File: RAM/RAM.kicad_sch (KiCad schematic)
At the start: 0 parts

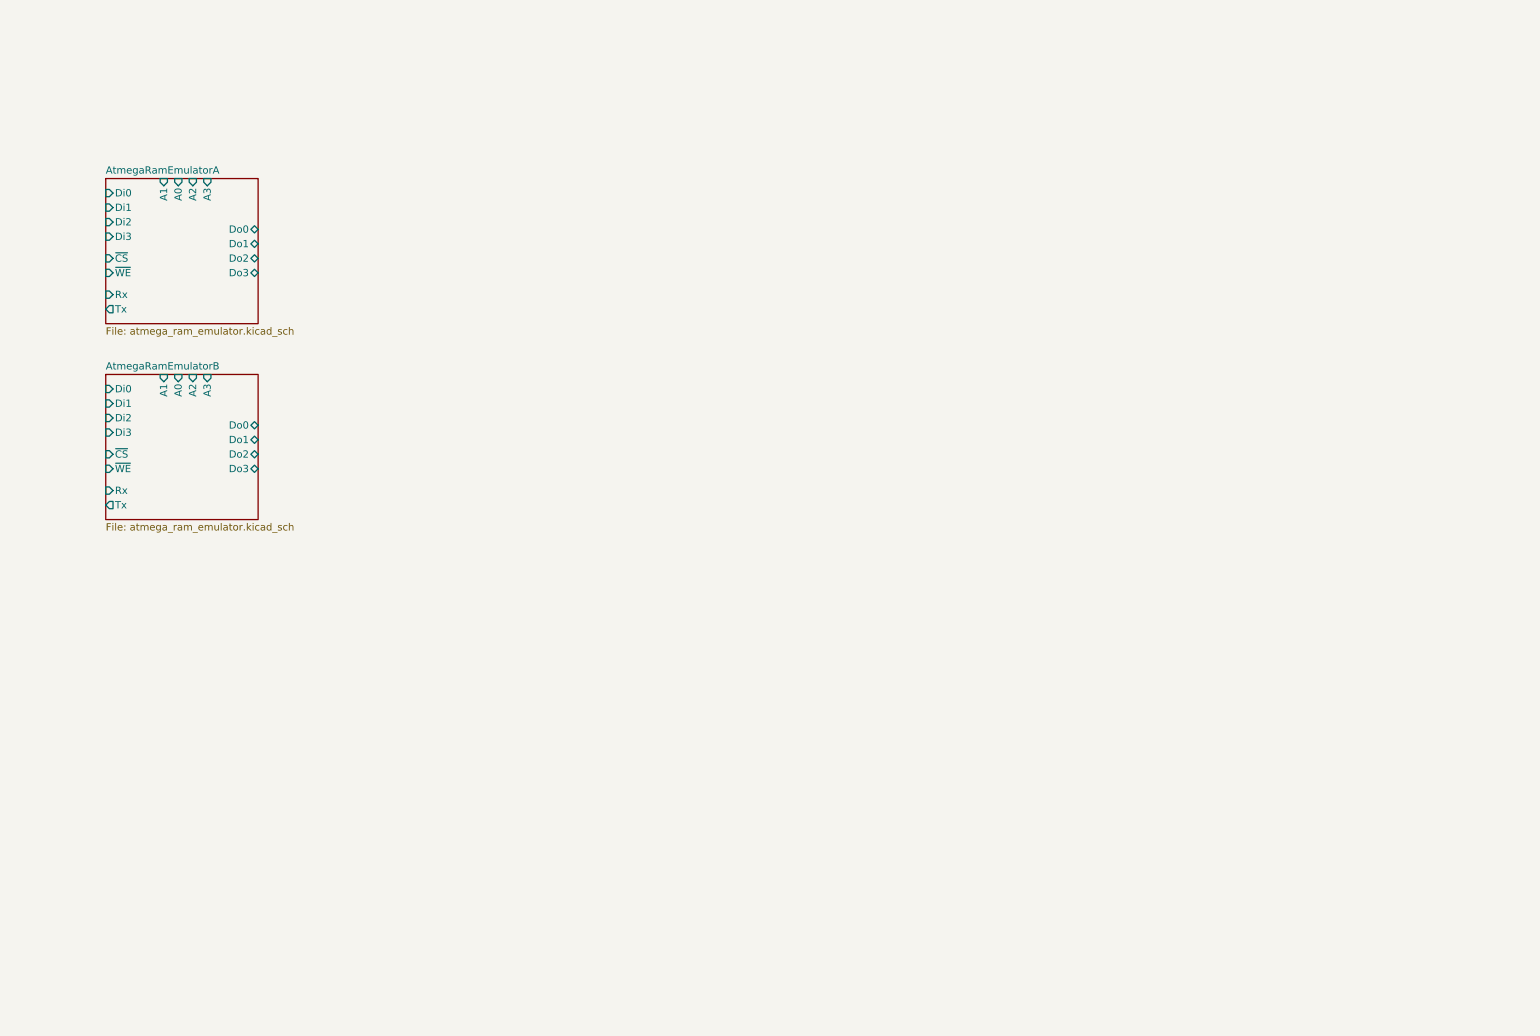
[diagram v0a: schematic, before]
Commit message: RAM input selection schematic complete
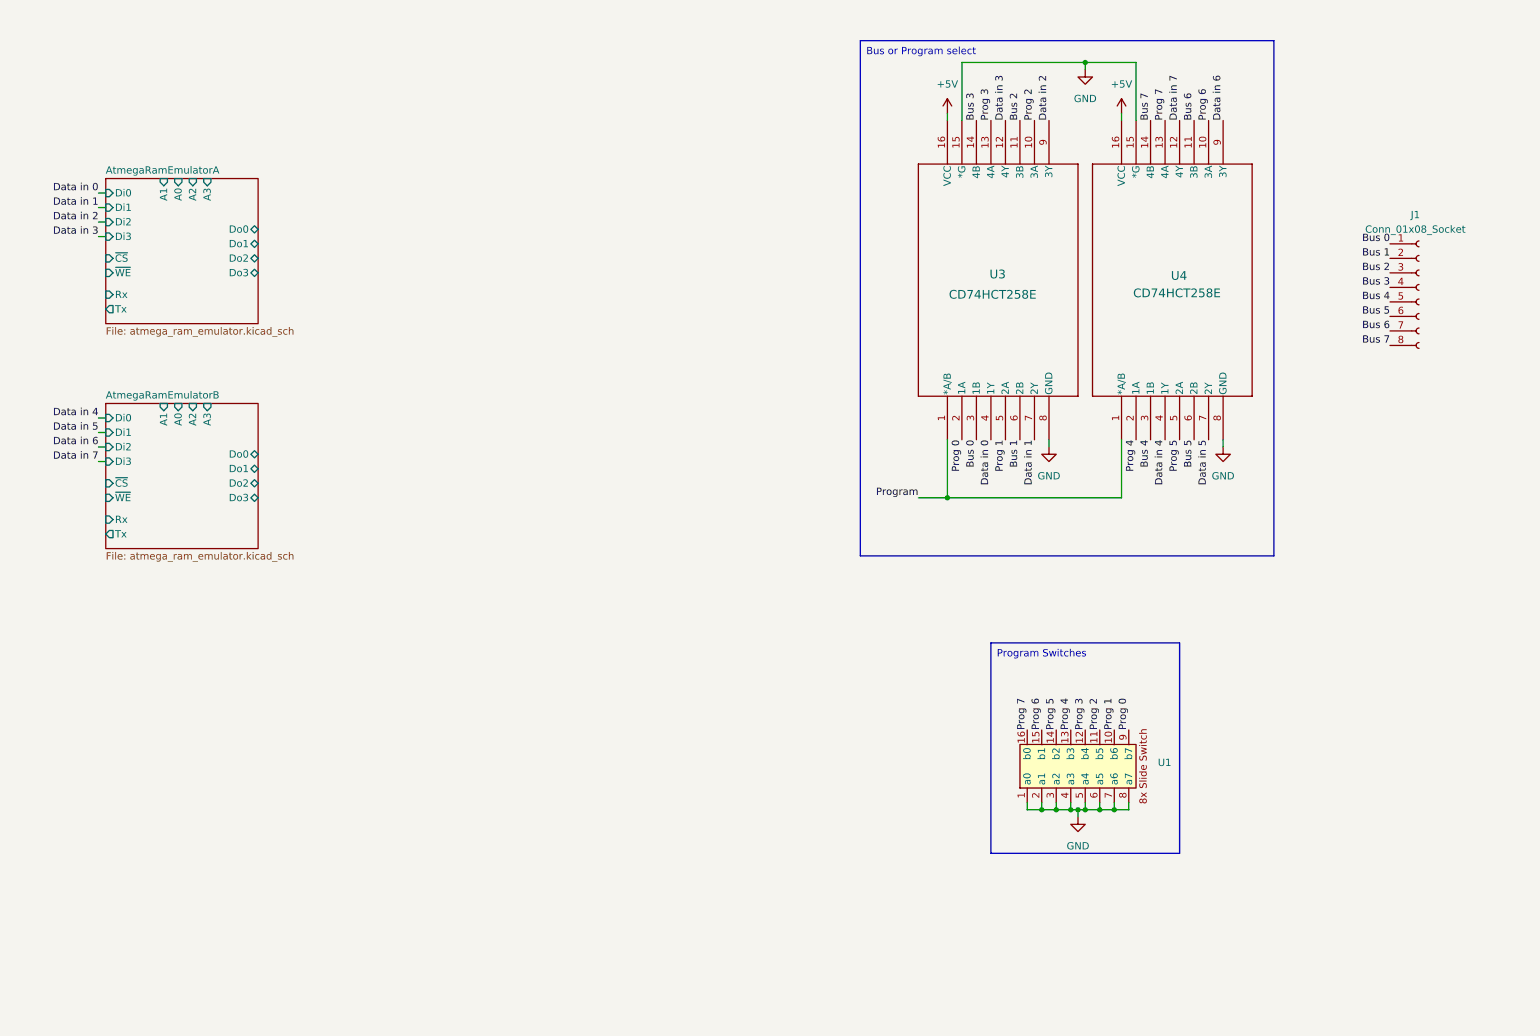
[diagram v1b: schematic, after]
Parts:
- added J1: Conn_01x08_Socket, Connector_PinHeader_1.00mm:PinHeader_1x08_P1.00mm_Horizontal, symbol Connector:Conn_01x08_Socket
- added U1: ~, symbol 8BitCPU:8x_slide_switch
- added U3, U4: CD74HCT258E, N16, symbol 2_to_1_selector:CD74HCT258E
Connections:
- new net +5V: U3.16 (VCC), U4.16 (VCC)
- new net Bus 0: J1.1 (Pin_1), U3.3 (1B)
- new net Bus 1: J1.2 (Pin_2), U3.6 (2B)
- new net Bus 2: J1.3 (Pin_3), U3.11 (3B)
- new net Bus 3: J1.4 (Pin_4), U3.14 (4B)
- new net Bus 4: J1.5 (Pin_5), U4.3 (1B)
- new net Bus 5: J1.6 (Pin_6), U4.6 (2B)
- new net Bus 6: J1.7 (Pin_7), U4.11 (3B)
- new net Bus 7: J1.8 (Pin_8), U4.14 (4B)
- new net Data in 0: U3.4 (1Y)
- new net Data in 1: U3.7 (2Y)
- new net Data in 2: U3.9 (3Y)
- new net Data in 3: U3.12 (4Y)
- new net Data in 4: U4.4 (1Y)
- new net Data in 5: U4.7 (2Y)
- new net Data in 6: U4.9 (3Y)
- new net Data in 7: U4.12 (4Y)
- new net GND: U1.1 (a0), U1.2 (a1), U1.3 (a2), U1.4 (a3), U1.5 (a4), U1.6 (a5), U1.7 (a6), U1.8 (a7), U3.15 (*G), U3.8 (GND), U4.15 (*G), U4.8 (GND)
- new net Prog 0: U1.9 (b7), U3.2 (1A)
- new net Prog 1: U1.10 (b6), U3.5 (2A)
- new net Prog 2: U1.11 (b5), U3.10 (3A)
- new net Prog 3: U1.12 (b4), U3.13 (4A)
- new net Prog 4: U1.13 (b3), U4.2 (1A)
- new net Prog 5: U1.14 (b2), U4.5 (2A)
- new net Prog 6: U1.15 (b1), U4.10 (3A)
- new net Prog 7: U1.16 (b0), U4.13 (4A)
- new net Program: U3.1 (*A/B), U4.1 (*A/B)

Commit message: RAM output connected to bus
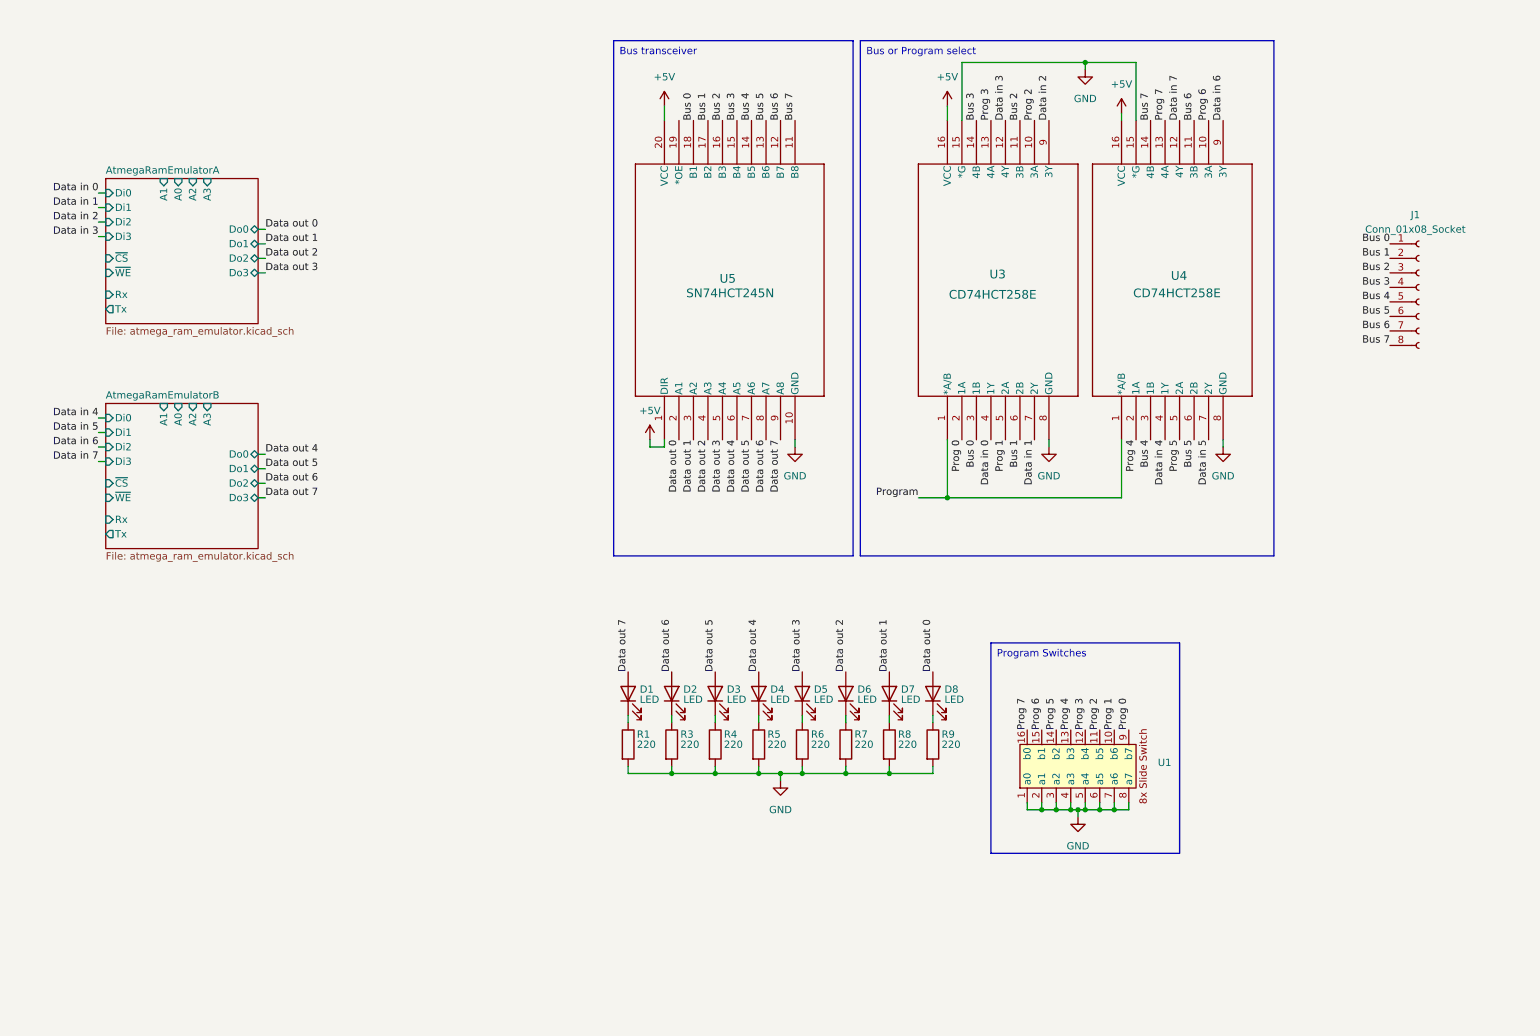
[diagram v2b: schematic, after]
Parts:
- added D1, D2, D3, D4, D5, D6, D7, D8: LED, LED_THT:LED_D2.0mm_W4.8mm_H2.5mm_FlatTop, symbol Device:LED
- added R1, R3, R4, R5, R6, R7, R8, R9: 220, _DownloadFootprints:CF_series_Resistors_THT, symbol Device:R
- added U5: SN74HCT245N, _DownloadFootprints:8x_tristate_transceiver, symbol 8x_tristate_transceiver:SN74HCT245N
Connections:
- net +5V: now also U5.1 (DIR), U5.20 (VCC)
- net Bus 0: now also U5.18 (B1)
- net Bus 1: now also U5.17 (B2)
- net Bus 2: now also U5.16 (B3)
- net Bus 3: now also U5.15 (B4)
- net Bus 4: now also U5.14 (B5)
- net Bus 5: now also U5.13 (B6)
- net Bus 6: now also U5.12 (B7)
- net Bus 7: now also U5.11 (B8)
- net GND: now also R1.2, R3.2, R4.2, R5.2, R6.2, R7.2, R8.2, R9.2, U5.10 (GND)
- new net: D7.1 (K), R8.1
- new net: D8.1 (K), R9.1
- new net: D4.1 (K), R5.1
- new net: D1.1 (K), R1.1
- new net: D6.1 (K), R7.1
- new net: D2.1 (K), R3.1
- new net: D3.1 (K), R4.1
- new net: D5.1 (K), R6.1
- new net Data out 0: D8.2 (A), U5.2 (A1)
- new net Data out 1: D7.2 (A), U5.3 (A2)
- new net Data out 2: D6.2 (A), U5.4 (A3)
- new net Data out 3: D5.2 (A), U5.5 (A4)
- new net Data out 4: D4.2 (A), U5.6 (A5)
- new net Data out 5: D3.2 (A), U5.7 (A6)
- new net Data out 6: D2.2 (A), U5.8 (A7)
- new net Data out 7: D1.2 (A), U5.9 (A8)

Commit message: Added logic to select between program or run mode signals
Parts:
- added C1: C, symbol Device:C
- added J2, J3: Conn_01x02_Pin, symbol Connector:Conn_01x02_Pin
- added J4: Conn_01x04_Pin, symbol Connector:Conn_01x04_Pin
- added R10: R, symbol Device:R
- added S1: B3U-1000P, _DownloadFootprints:tactile_switch, symbol dk_Tactile-Switches:B3U-1000P
- added U6: CD74HCT258E, N16, symbol 2_to_1_selector:CD74HCT258E
- added U7: ~, symbol 8BitCPU:4x_and
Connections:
- net +5V: now also U6.16 (VCC), U7.14 (VCC)
- net AtmegaRamEmulatorA/Rx: now also J3.1 (Pin_1)
- net AtmegaRamEmulatorA/Tx: now also J3.2 (Pin_2)
- net AtmegaRamEmulatorA/~{WE}: now also U6.12 (4Y)
- net AtmegaRamEmulatorB/Rx: now also J2.1 (Pin_1)
- net AtmegaRamEmulatorB/Tx: now also J2.2 (Pin_2)
- net GND: now also R10.2, S1.2, U6.15 (*G), U6.8 (GND), U7.7 (GND)
- net Program: now also J4.1 (Pin_1), U6.1 (*A/B)
- new net: C1.2, R10.1, U7.1 (1A)
- new net: S1.1, U6.13 (4A)
- new net: U6.14 (4B), U7.3 (1Y)
- new net CLK: C1.1, J4.2 (Pin_2)
- new net Read in: J4.4 (Pin_4), U7.2 (1B)
- new net ~Read out: J4.3 (Pin_3)
- no-connect marks 0 -> 18

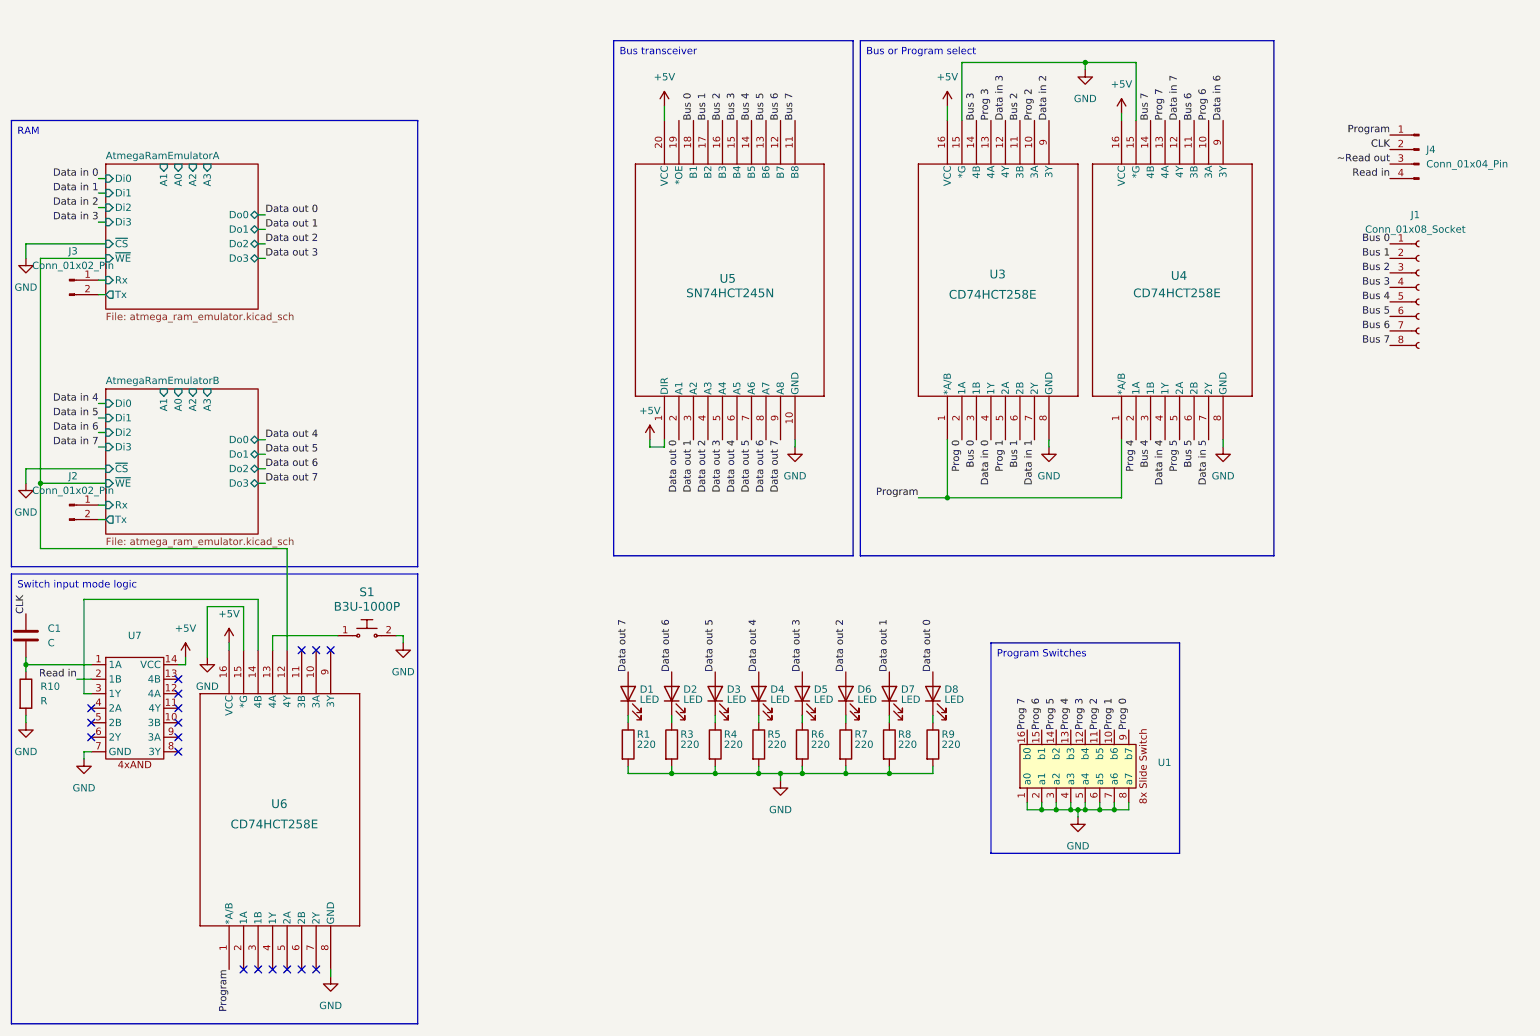
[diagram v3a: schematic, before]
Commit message: RAM schematic complete
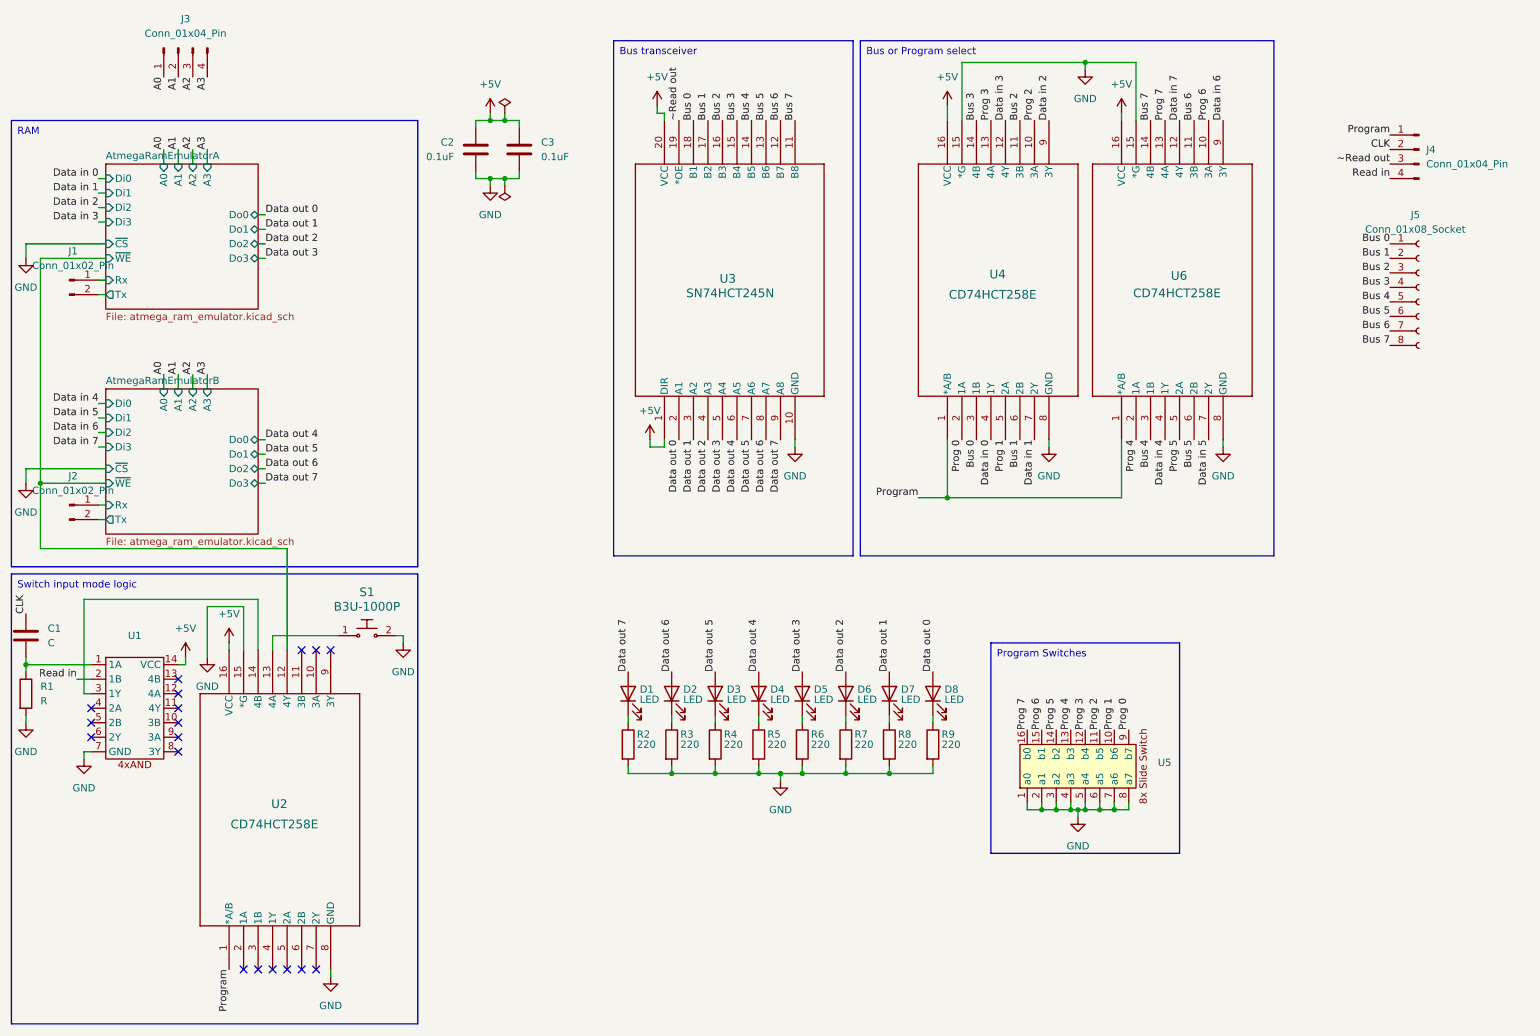
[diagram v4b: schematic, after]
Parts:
- added C2, C3: 0.1uF, Capacitor_THT:C_Disc_D5.0mm_W2.5mm_P2.50mm, symbol Device:C
- added J3: Conn_01x04_Pin, symbol Connector:Conn_01x04_Pin
- renumbered J3 to J1, J1 to J5, R10 to R1, R1 to R2, U7 to U1, U6 to U2, U5 to U3, U3 to U4, U1 to U5, U4 to U6
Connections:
- net +5V: now also C2.1, C3.1
- net GND: now also C2.2, C3.2
- net ~Read out: now also U3.19 (*OE)
- new net A0: J3.1 (Pin_1)
- new net A1: J3.2 (Pin_2)
- new net A2: J3.3 (Pin_3)
- new net A3: J3.4 (Pin_4)
